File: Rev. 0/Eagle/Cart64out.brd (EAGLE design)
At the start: 86 x 62 mm, 10 parts, among them J1 C64-EXPANSIONP, J3 C64-EXPANSION_F, SW1 JTP-1130

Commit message: Silk Screen Update
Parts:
- added U$22: OPEN_SOURCE_HW, Logo:OPENHW
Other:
- board text added: "8x10k"
- board text added: "http://github.com/ svenpetersen1965"

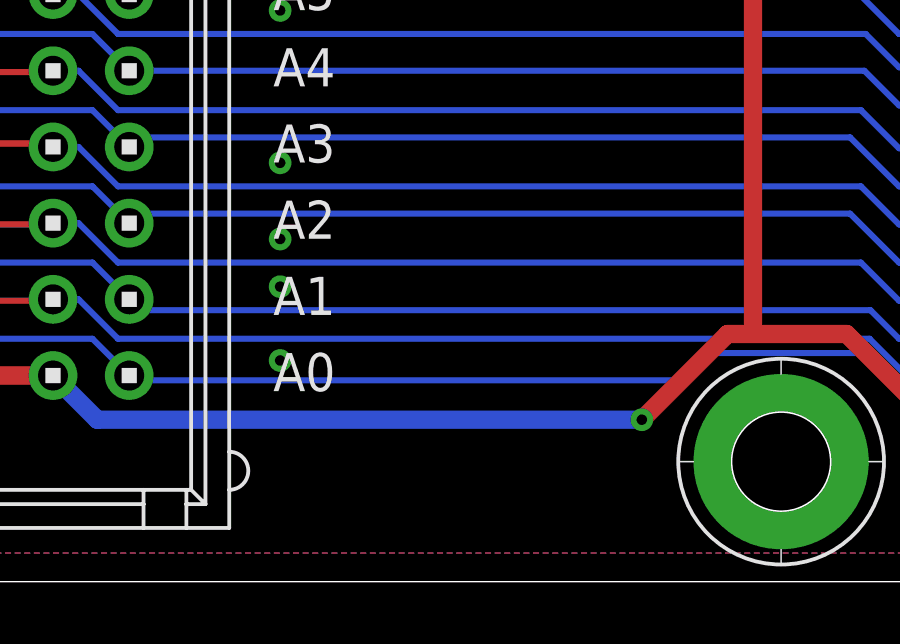
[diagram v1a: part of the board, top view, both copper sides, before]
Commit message: Doc Update
New dimensions added
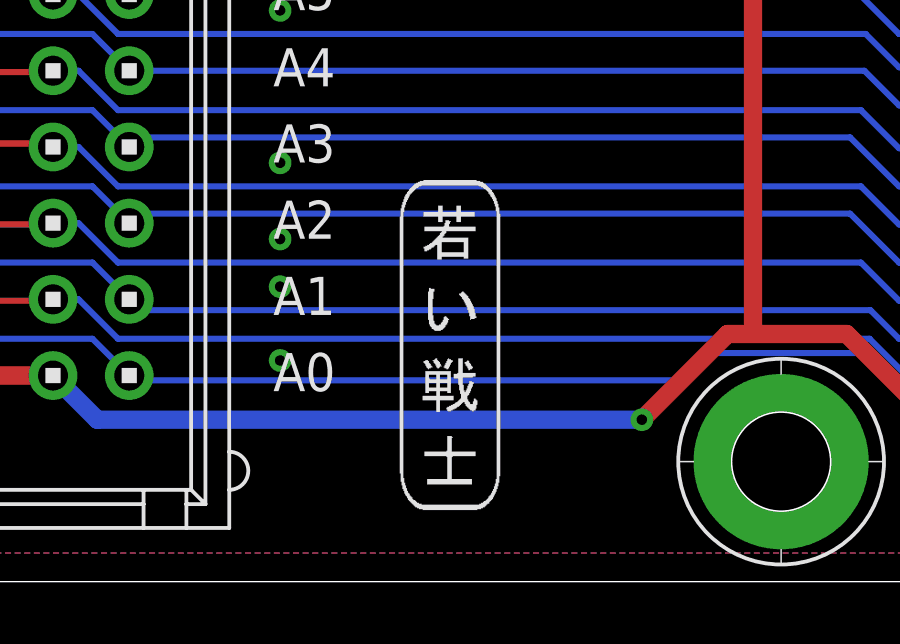
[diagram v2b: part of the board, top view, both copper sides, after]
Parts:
- added U$23: (no value), Logo:SVEN_TAG
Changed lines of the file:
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@@
 <?xml version="1.0" encoding="utf-8"?>
 <!DOCTYPE eagle SYSTEM "eagle.dtd">
-<eagle version="9.5.2">
+<eagle version="9.6.2">
 <drawing>
 <settings>
@@
 <setting verticaltext="up"/>
 </settings>
-<grid distance="3.125" unitdist="mil" unit="mil" style="lines" multiple="10" display="yes" altdistance="5" altunitdist="mil" altunit="mil"/>
+<grid distance="1" unitdist="mm" unit="mm" style="lines" multiple="10" display="yes" altdistance="5" altunitdist="mil" altunit="mil"/>
 <layers>
 <layer number="1" name="Top" color="4" fill="1" visible="no" active="yes"/>
@@
 svenpetersen1965</text>
 <text x="73.263125" y="27.94" size="1.27" layer="21" font="vector" ratio="11" rot="R270">8x10k</text>
+<dimension x1="48" y1="31" x2="0" y2="31" x3="24" y3="-3.81" textsize="1.27" textratio="11" layer="47" dtype="horizontal"/>
+<wire x1="0" y1="31" x2="97" y2="31" width="0.127" layer="47" style="dashdot"/>
 </plain>
 <attributes>
@@
 </element>
 <element name="U$22" library="Logo" package="OPENHW" value="OPEN_SOURCE_HW" x="26.67" y="6.429375" smashed="yes" rot="R90"/>
+<element name="U$23" library="Logo" package="SVEN_TAG" value="" x="60" y="8" smashed="yes"/>
 </elements>
 <signals>
